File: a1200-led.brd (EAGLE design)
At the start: 34.1 x 28 mm, 10 parts

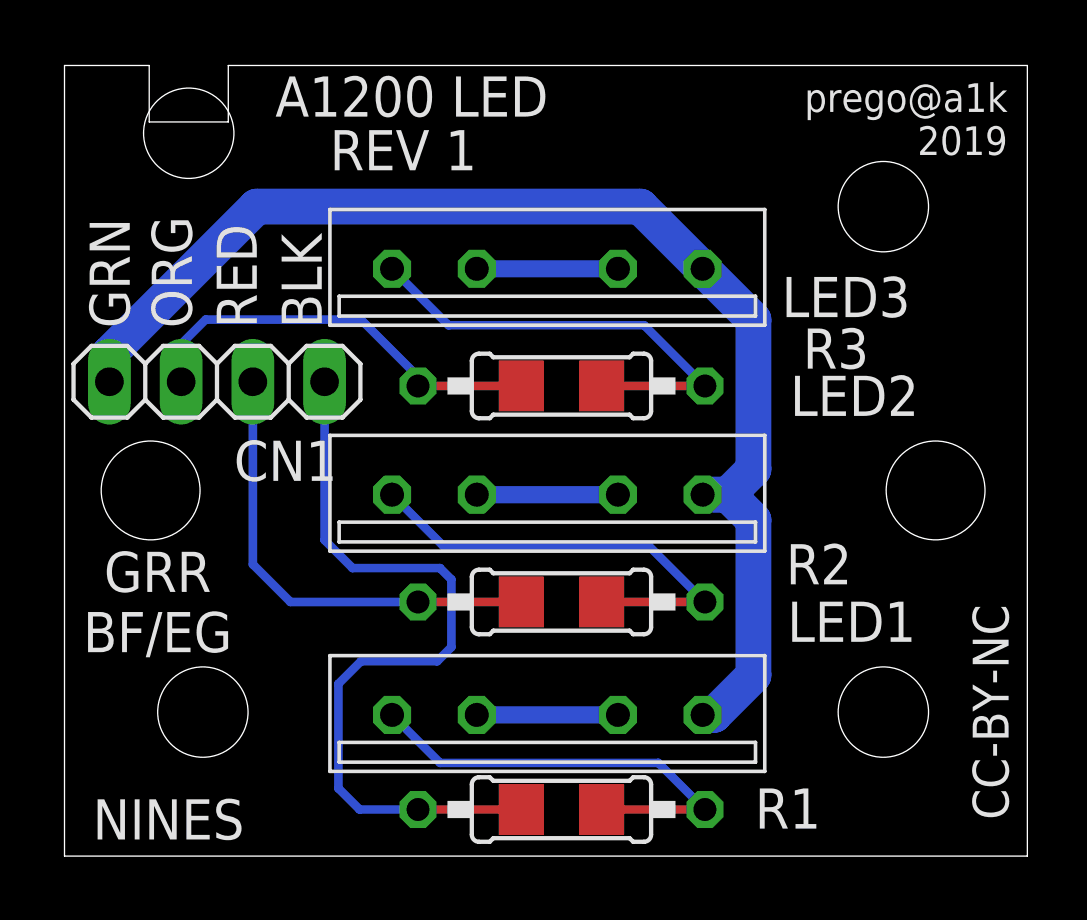
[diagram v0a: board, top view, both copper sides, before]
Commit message: fixed led pin width, v0.2
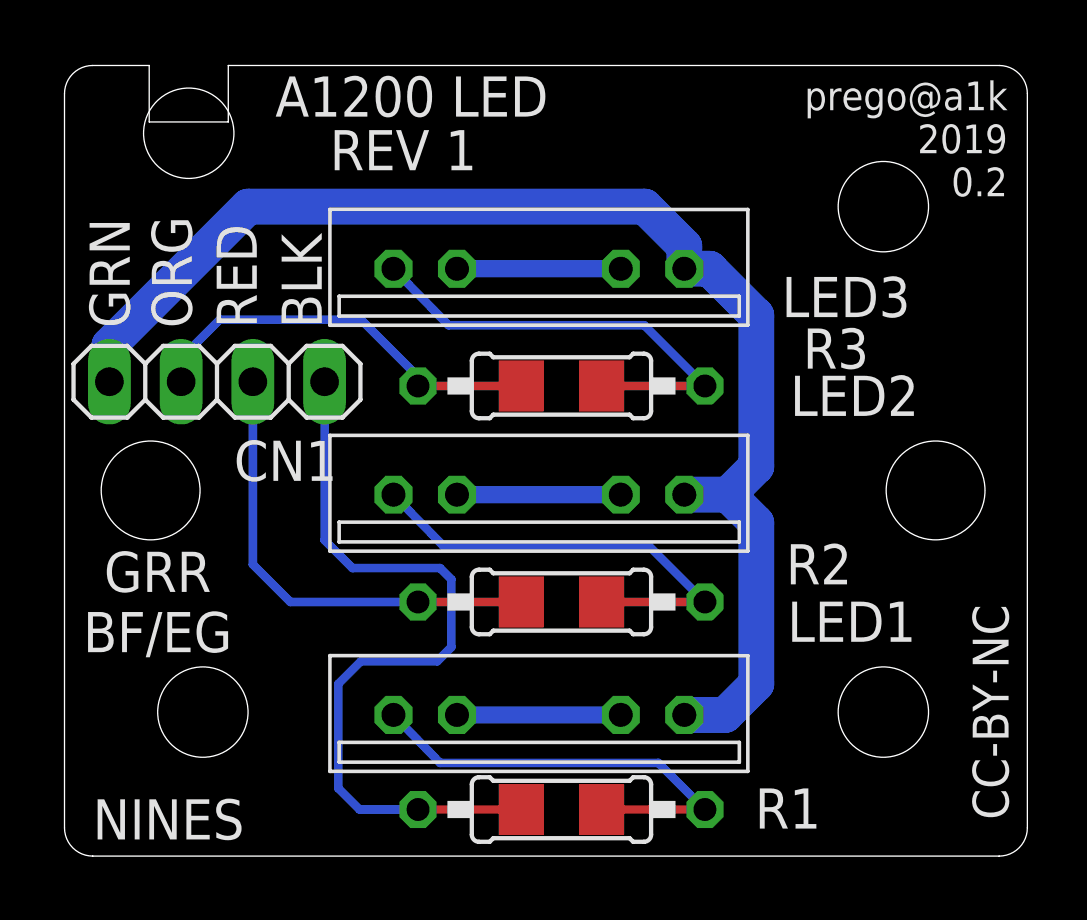
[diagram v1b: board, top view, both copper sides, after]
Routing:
- net GND: track 44.2 -> 46.7 mm
- net N$8: track 5.00 -> 5.80 mm
- net N$5: track 5.00 -> 5.80 mm
- net N$2: track 5.00 -> 5.80 mm
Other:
- outline, holes or cut-outs redrawn
- board text added: "prego@a1k 2019 0.2"
- board text removed: "prego@a1k 2019"
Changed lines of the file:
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@@
 <board>
 <plain>
-<wire x1="0" y1="0" x2="34.1" y2="0" width="0" layer="20"/>
-<wire x1="34.1" y1="0" x2="34.1" y2="28" width="0" layer="20"/>
-<wire x1="34.1" y1="28" x2="5.8" y2="28" width="0" layer="20"/>
+<wire x1="1" y1="0" x2="33.1" y2="0" width="0" layer="20"/>
+<wire x1="33.1" y1="0" x2="34.1" y2="1" width="0" layer="20" curve="90"/>
+<wire x1="34.1" y1="1" x2="34.1" y2="27" width="0" layer="20"/>
+<wire x1="34.1" y1="27" x2="33.1" y2="28" width="0" layer="20" curve="90"/>
+<wire x1="33.1" y1="28" x2="5.8" y2="28" width="0" layer="20"/>
 <wire x1="5.8" y1="28" x2="5.8" y2="26" width="0" layer="20"/>
 <wire x1="5.8" y1="26" x2="3" y2="26" width="0" layer="20"/>
 <wire x1="3" y1="26" x2="3" y2="28" width="0" layer="20"/>
-<wire x1="3" y1="28" x2="0" y2="28" width="0" layer="20"/>
-<wire x1="0" y1="28" x2="0" y2="0" width="0" layer="20"/>
+<wire x1="3" y1="28" x2="1" y2="28" width="0" layer="20"/>
+<wire x1="1" y1="28" x2="0" y2="27" width="0" layer="20" curve="90"/>
+<wire x1="0" y1="27" x2="0" y2="1" width="0" layer="20"/>
+<wire x1="0" y1="1" x2="1" y2="0" width="0" layer="20" curve="90"/>
 <hole x="4.9" y="5.1" drill="3.2"/>
 <hole x="29" y="5.1" drill="3.2"/>
@@
 <text x="6.1" y="18.7" size="1.4224" layer="25" font="vector" ratio="7" rot="R90" align="center-left">RED</text>
 <text x="8.4" y="18.7" size="1.4224" layer="25" font="vector" ratio="7" rot="R90" align="center-left">BLK</text>
-<text x="33.4" y="26.1" size="1.016" layer="25" font="vector" ratio="7" align="center-right">prego@a1k
-2019</text>
+<text x="33.4" y="25.4" size="1.016" layer="25" font="vector" ratio="7" align="center-right">prego@a1k
+2019
+0.2</text>
 <text x="1" y="1.3" size="1.4224" layer="25" font="vector" ratio="7" align="center-left">NINES</text>
 <text x="6" y="14" size="1.4224" layer="25" font="vector" ratio="7" align="center-left">CN1</text>
@@
 <wire x1="19.022" y1="1.65" x2="22.68" y2="1.65" width="0.3048" layer="1"/>
 <wire x1="22.68" y1="1.65" x2="21.03" y2="3.3" width="0.3048" layer="16"/>
-<wire x1="13.3" y1="3.3" x2="11.6" y2="5" width="0.3048" layer="16"/>
+<wire x1="13.3" y1="3.3" x2="11.65" y2="5" width="0.3048" layer="16"/>
 <wire x1="21.03" y1="3.3" x2="13.3" y2="3.3" width="0.3048" layer="16"/>
 </signal>
@@
 <contactref element="LED1" pad="LED-OUT1"/>
 <contactref element="LED1" pad="LED-IN2"/>
-<wire x1="14.6" y1="5" x2="19.6" y2="5" width="0.6096" layer="16"/>
+<wire x1="13.9" y1="5" x2="19.7" y2="5" width="0.6096" layer="16"/>
 </signal>
 <signal name="GND">
@@
 <contactref element="LED3" pad="LED-OU2"/>
 <contactref element="JP1" pad="1"/>
-<wire x1="1.59" y1="16.8" x2="1.59" y2="17.79" width="1.27" layer="16"/>
-<wire x1="1.59" y1="17.79" x2="6.8" y2="23" width="1.27" layer="16"/>
-<wire x1="6.8" y1="23" x2="20.4" y2="23" width="1.27" layer="16"/>
-<wire x1="20.4" y1="23" x2="22.6" y2="20.8" width="1.27" layer="16"/>
-<wire x1="22.6" y1="20.8" x2="24.4" y2="19" width="1.27" layer="16"/>
-<wire x1="24.4" y1="19" x2="24.4" y2="13.7" width="1.27" layer="16"/>
-<wire x1="23.5" y1="12.8" x2="24.4" y2="13.7" width="1.27" layer="16"/>
-<wire x1="22.6" y1="12.8" x2="23.5" y2="12.8" width="1.27" layer="16"/>
-<wire x1="23.5" y1="12.8" x2="24.4" y2="11.9" width="1.27" layer="16"/>
-<wire x1="24.4" y1="11.9" x2="24.4" y2="6.4" width="1.27" layer="16"/>
-<wire x1="24.4" y1="6.4" x2="23" y2="5" width="1.27" layer="16"/>
-<wire x1="23" y1="5" x2="22.6" y2="5" width="1.27" layer="16"/>
+<wire x1="1.59" y1="16.8" x2="1.59" y2="18.09" width="1.27" layer="16"/>
+<wire x1="1.59" y1="18.09" x2="6.5" y2="23" width="1.27" layer="16"/>
+<wire x1="24.5" y1="19.15" x2="22.85" y2="20.8" width="1.27" layer="16"/>
+<wire x1="21.95" y1="20.8" x2="22.85" y2="20.8" width="1.27" layer="16"/>
+<wire x1="24.5" y1="19.15" x2="24.5" y2="13.8" width="1.27" layer="16"/>
+<wire x1="23.5" y1="12.8" x2="24.5" y2="13.8" width="1.27" layer="16"/>
+<wire x1="21.95" y1="12.8" x2="23.5" y2="12.8" width="1.27" layer="16"/>
+<wire x1="23.5" y1="12.8" x2="24.5" y2="11.8" width="1.27" layer="16"/>
+<wire x1="24.5" y1="11.8" x2="24.5" y2="6.1" width="1.27" layer="16"/>
+<wire x1="24.5" y1="6.1" x2="23.4" y2="5" width="1.27" layer="16"/>
+<wire x1="23.4" y1="5" x2="21.95" y2="5" width="1.27" layer="16"/>
+<wire x1="21.95" y1="21.6" x2="21.95" y2="20.8" width="1.27" layer="16"/>
+<wire x1="21.95" y1="21.6" x2="20.55" y2="23" width="1.27" layer="16"/>
+<wire x1="6.5" y1="23" x2="20.55" y2="23" width="1.27" layer="16"/>
 </signal>
 <signal name="N$4">
@@
 <wire x1="19.022" y1="9" x2="22.68" y2="9" width="0.3048" layer="1"/>
 <wire x1="22.68" y1="9" x2="20.68" y2="11" width="0.3048" layer="16"/>
-<wire x1="13.4" y1="11" x2="11.6" y2="12.8" width="0.3048" layer="16"/>
+<wire x1="13.4" y1="11" x2="11.65" y2="12.8" width="0.3048" layer="16"/>
 <wire x1="20.68" y1="11" x2="13.4" y2="11" width="0.3048" layer="16"/>
 </signal>
@@
 <contactref element="LED2" pad="LED-OUT1"/>
 <contactref element="LED2" pad="LED-IN2"/>
-<wire x1="14.6" y1="12.8" x2="19.6" y2="12.8" width="0.6096" layer="16"/>
+<wire x1="13.9" y1="12.8" x2="19.7" y2="12.8" width="0.6096" layer="16"/>
 </signal>
 <signal name="N$7">
@@
 <wire x1="19.022" y1="16.65" x2="22.68" y2="16.65" width="0.3048" layer="1"/>
 <wire x1="22.68" y1="16.65" x2="20.53" y2="18.8" width="0.3048" layer="16"/>
-<wire x1="13.6" y1="18.8" x2="11.6" y2="20.8" width="0.3048" layer="16"/>
+<wire x1="13.6" y1="18.8" x2="11.65" y2="20.8" width="0.3048" layer="16"/>
 <wire x1="20.53" y1="18.8" x2="13.6" y2="18.8" width="0.3048" layer="16"/>
 </signal>
@@
 <contactref element="LED3" pad="LED-OUT1"/>
 <contactref element="LED3" pad="LED-IN2"/>
-<wire x1="14.6" y1="20.8" x2="19.6" y2="20.8" width="0.6096" layer="16"/>
+<wire x1="13.9" y1="20.8" x2="19.7" y2="20.8" width="0.6096" layer="16"/>
 </signal>
 <signal name="RED">
@@
 <contactref element="R6" pad="1"/>
 <contactref element="JP1" pad="2"/>
-<wire x1="4.13" y1="16.8" x2="4.13" y2="18.13" width="0.3048" layer="16"/>
-<wire x1="4.13" y1="18.13" x2="5" y2="19" width="0.3048" layer="16"/>
-<wire x1="5" y1="19" x2="10.5" y2="19" width="0.3048" layer="16"/>
+<wire x1="4.13" y1="16.8" x2="4.13" y2="17.63" width="0.3048" layer="16"/>
+<wire x1="4.13" y1="17.63" x2="5.5" y2="19" width="0.3048" layer="16"/>
+<wire x1="5.5" y1="19" x2="10.5" y2="19" width="0.3048" layer="16"/>
 <wire x1="10.5" y1="19" x2="12.5" y2="17" width="0.3048" layer="16"/>
 <wire x1="12.5" y1="17" x2="12.5" y2="16.67" width="0.3048" layer="16"/>
